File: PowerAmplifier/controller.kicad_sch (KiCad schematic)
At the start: 53 parts, among them J13 VADJ, J14 I2C, J15 SWD, U10 TPSM861252, U11 LP38798, U3 TLV4387, U4 INA241A2xDGK, U5 INA241A2xDGK, U6 INA241A2xDGK, U7 INA241A2xDGK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

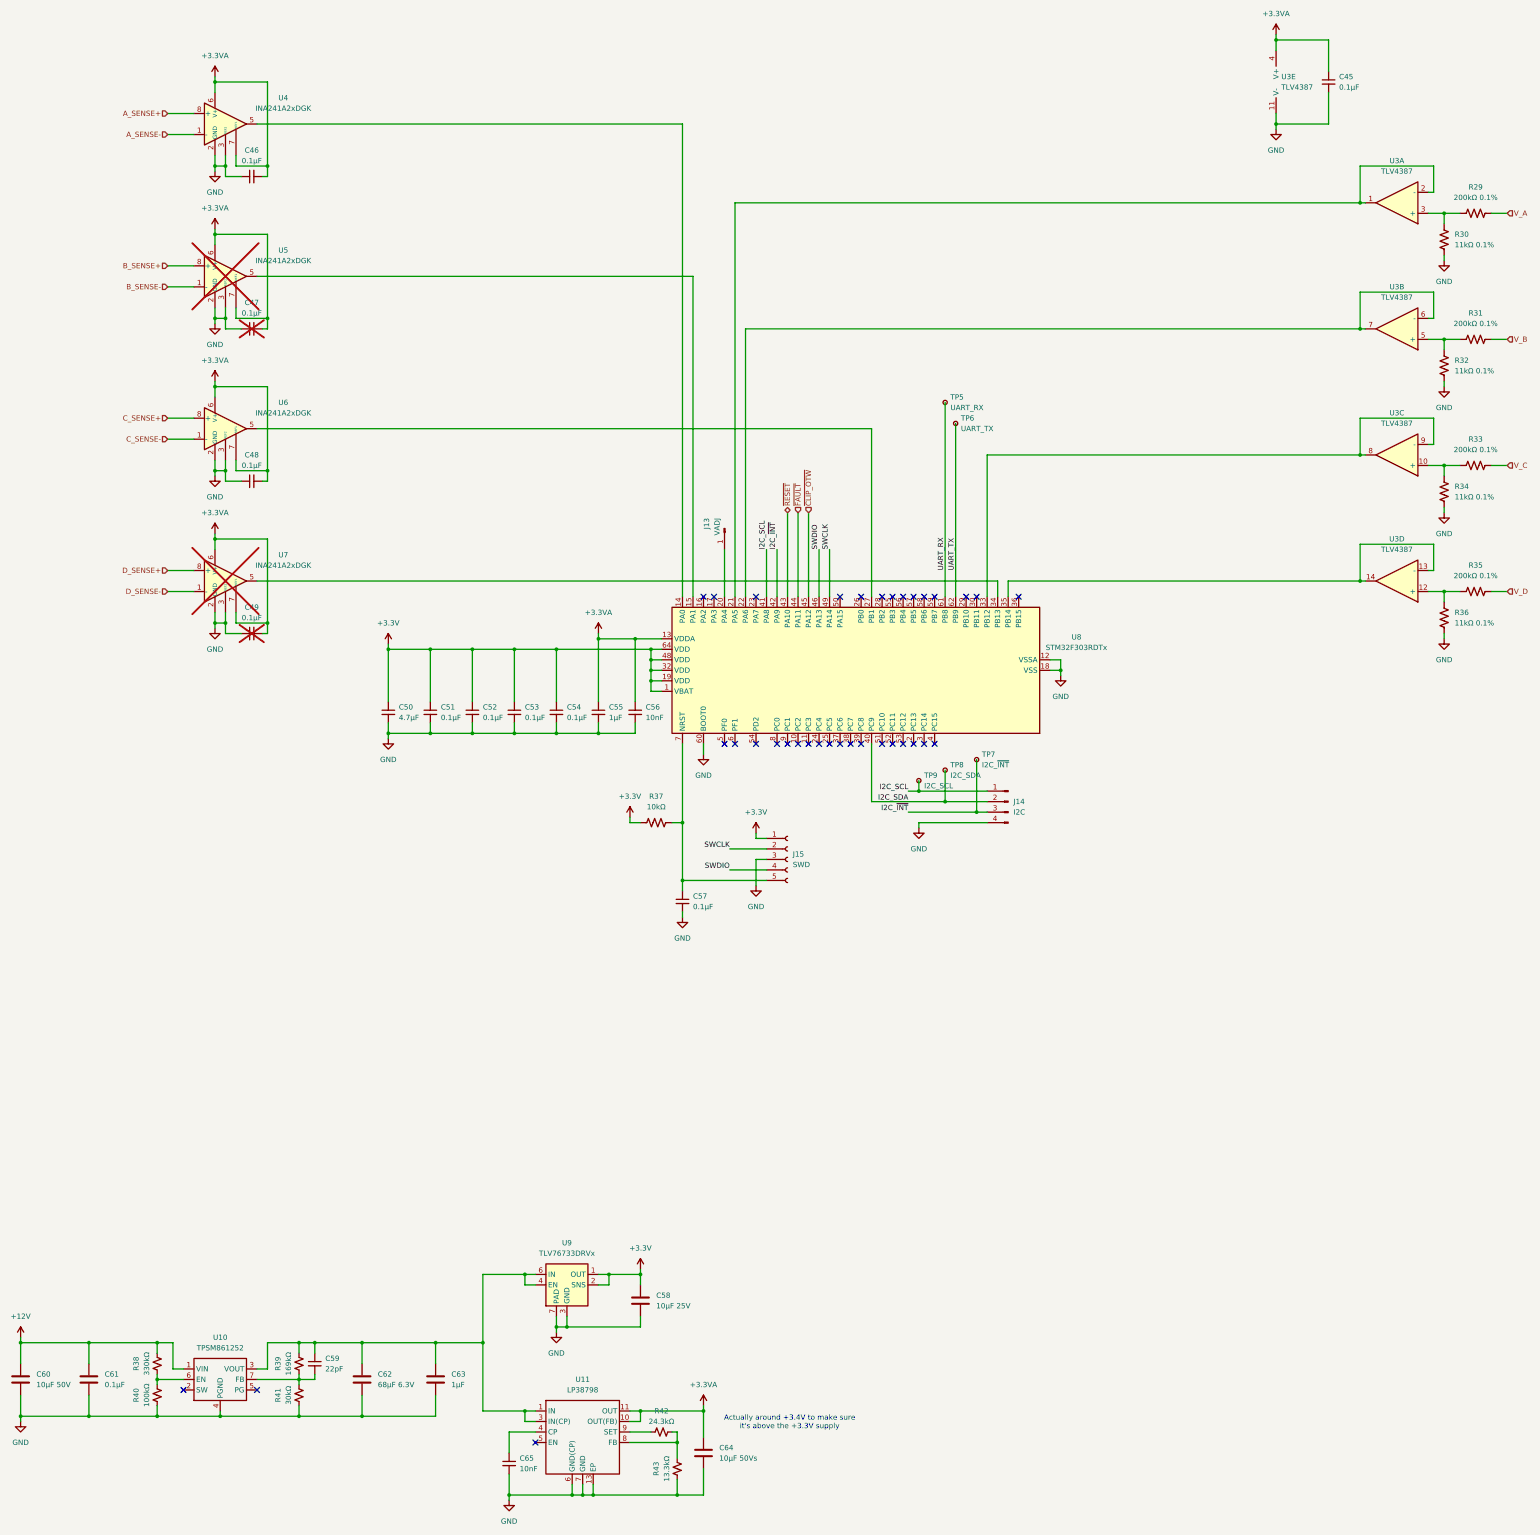
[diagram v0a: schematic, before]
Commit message: PowerAmplifier initially complete, PowerAmpSupply progress
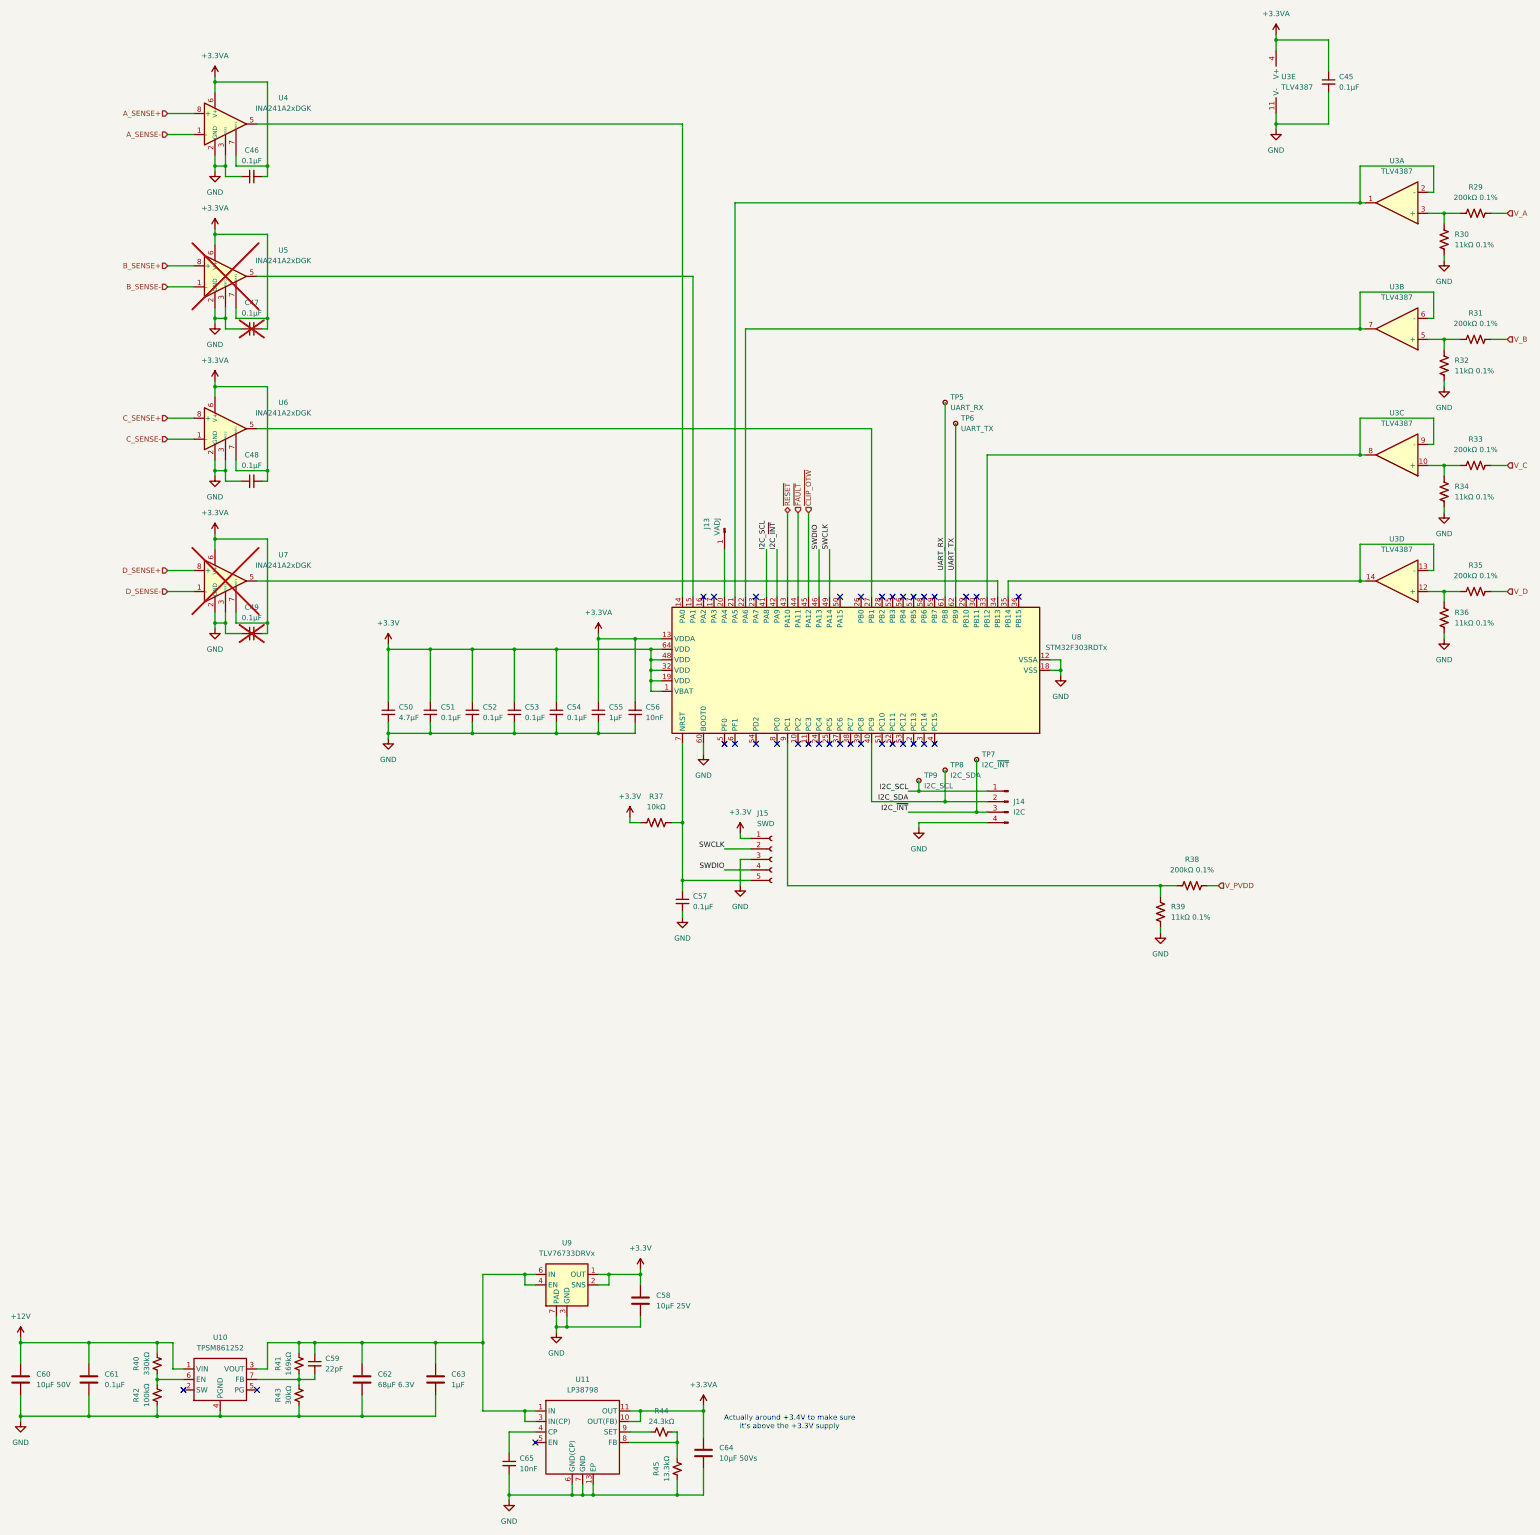
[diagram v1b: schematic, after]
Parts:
- added R38: 200kΩ 0.1%, Resistor_SMD:R_0603_1608Metric, symbol Device:R_US
- added R39: 11kΩ 0.1%, Resistor_SMD:R_0603_1608Metric, symbol Device:R_US
- renumbered R38 to R40, R39 to R41, R40 to R42, R41 to R43, R42 to R44, R43 to R45
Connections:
- net GND: now also R39.1
- net at U8.9 (PC1): now also R38.2, R39.2
- new net V_PVDD: R38.1
- no-connect marks 35 -> 34
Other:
- moved on the sheet: J15

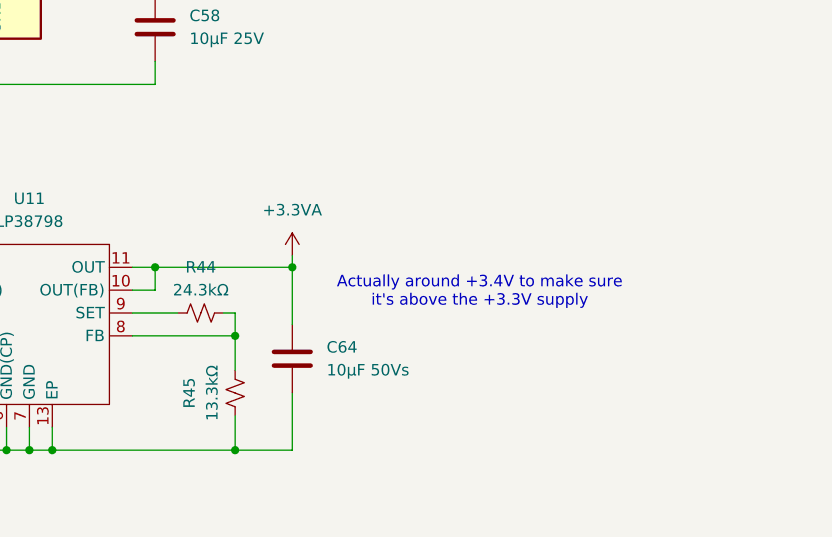
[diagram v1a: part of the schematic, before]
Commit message: PowerAmpSupply VTRK change
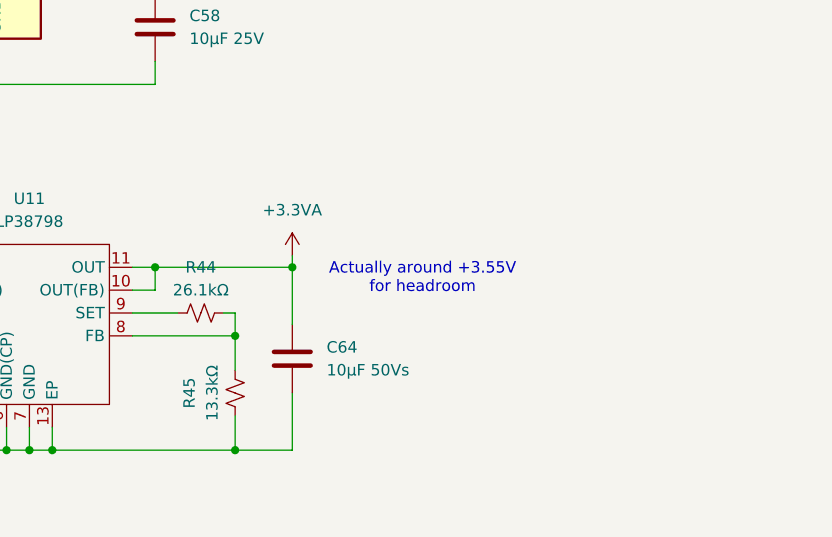
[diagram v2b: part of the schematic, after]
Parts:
- R44: value 24.3kΩ -> 26.1kΩ
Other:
- note added: "Actually around +3.55V for headroom"
- note removed: "Actually around +3.4V to make sure it's above the +3.3V supply"
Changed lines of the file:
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@@
 		)
 	)
-	(text "Actually around +3.4V to make sure\nit's above the +3.3V supply"
+	(text "Actually around +3.55V\nfor headroom"
 		(exclude_from_sim no)
-		(at 217.678 368.554 0)
+		(at 211.328 367.03 0)
 		(effects
 			(font
@@
 			)
 		)
-		(property "Value" "24.3kΩ"
+		(property "Value" "26.1kΩ"
 			(at 186.69 368.3 90)
 			(effects
